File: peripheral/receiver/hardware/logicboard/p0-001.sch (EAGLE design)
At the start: 14 parts, among them IC1 74LS07N, IC2 LTC485N

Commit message: Clean up of document, schematic, and board design.
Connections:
- net GND: no longer JP1.3, MIDIOUT.3
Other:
- note added: "NC"
- note removed: "MIDI Receiver Selector"
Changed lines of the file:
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@@
 <setting verticaltext="up"/>
 </settings>
-<grid distance="0.1" unitdist="inch" unit="inch" style="dots" multiple="1" display="yes" altdistance="0.01" altunitdist="inch" altunit="inch"/>
+<grid distance="0.1" unitdist="inch" unit="inch" style="lines" multiple="1" display="no" altdistance="0.01" altunitdist="inch" altunit="inch"/>
 <layers>
 <layer number="1" name="Top" color="4" fill="1" visible="no" active="no"/>
@@
 <text x="38.1" y="139.7" size="1.778" layer="97" rot="R90">GND</text>
 <text x="40.64" y="139.7" size="1.778" layer="97" rot="R90">External Vcc</text>
-<text x="35.56" y="139.7" size="1.778" layer="97" rot="R90">MIDI Receiver Selector</text>
+<text x="35.56" y="139.7" size="1.778" layer="97" rot="R90">NC</text>
 <text x="33.02" y="139.7" size="1.778" layer="97" rot="R90">MIDI OUT Send</text>
 <text x="30.48" y="139.7" size="1.778" layer="97" rot="R90">MIDI OUT Return</text>
@@
 <wire x1="38.1" y1="116.84" x2="50.8" y2="116.84" width="0.1524" layer="91"/>
 <wire x1="50.8" y1="116.84" x2="50.8" y2="88.9" width="0.1524" layer="91"/>
-<wire x1="38.1" y1="134.62" x2="38.1" y2="121.92" width="0.1524" layer="91"/>
+<wire x1="38.1" y1="134.62" x2="38.1" y2="116.84" width="0.1524" layer="91"/>
 <junction x="38.1" y="116.84"/>
 <pinref part="JP1" gate="A" pin="2"/>
-<pinref part="MIDIOUT" gate="G$1" pin="3"/>
-<pinref part="JP1" gate="A" pin="3"/>
-<wire x1="38.1" y1="121.92" x2="38.1" y2="116.84" width="0.1524" layer="91"/>
-<wire x1="35.56" y1="134.62" x2="35.56" y2="121.92" width="0.1524" layer="91"/>
-<wire x1="35.56" y1="121.92" x2="25.4" y2="121.92" width="0.1524" layer="91"/>
-<wire x1="25.4" y1="121.92" x2="25.4" y2="104.14" width="0.1524" layer="91"/>
-<wire x1="25.4" y1="104.14" x2="27.94" y2="104.14" width="0.1524" layer="91"/>
-<wire x1="38.1" y1="121.92" x2="35.56" y2="121.92" width="0.1524" layer="91"/>
-<junction x="38.1" y="121.92"/>
-<junction x="35.56" y="121.92"/>
-</segment>
-<segment>
+</segment>
+<segment>

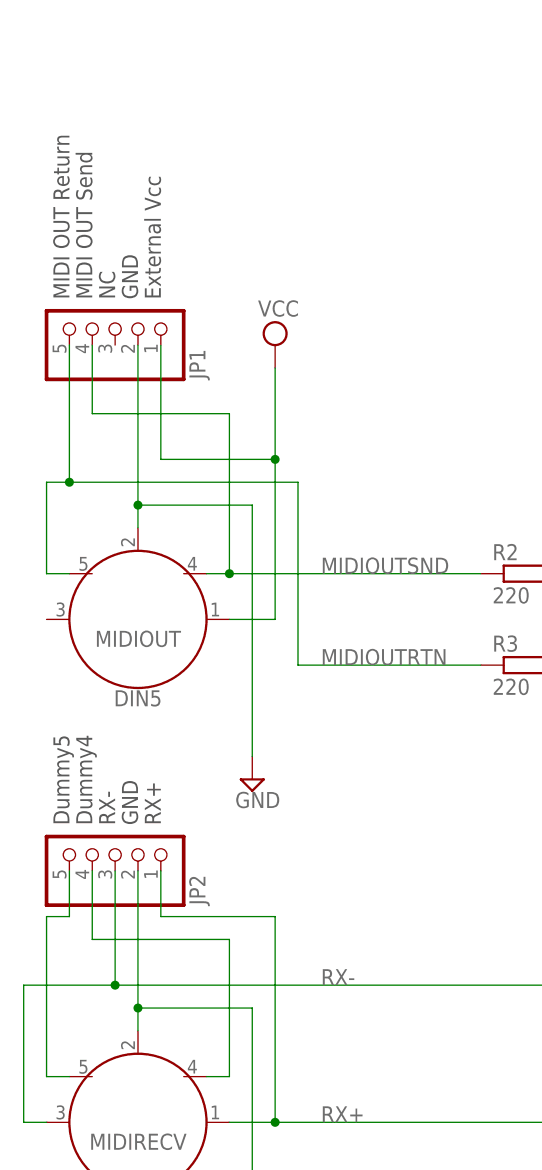
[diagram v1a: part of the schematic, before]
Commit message: Changed connectors of longrange receiver.
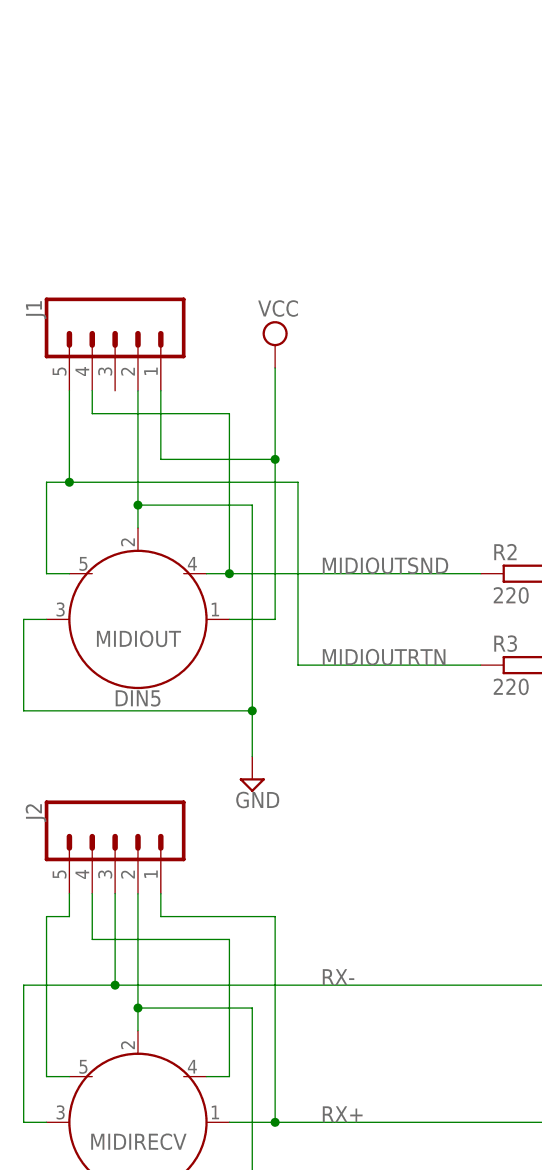
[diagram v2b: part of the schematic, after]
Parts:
- removed JP1, JP2: (no value), pinhead:PINHD-1X5
- added J1, J2: (no value), SparkFun-Connectors:CONN_05JST
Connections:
- net DUMMY4: now also J2.4; no longer JP2.4
- net DUMMY5: now also J2.5; no longer JP2.5
- net GND: now also J1.2, J2.2, MIDIOUT.3; no longer JP1.2, JP2.2
- net MIDIOUTRTN: now also J1.5; no longer JP1.5
- net MIDIOUTSND: now also J1.4; no longer JP1.4
- net RX+: now also J2.1; no longer JP2.1
- net RX-: now also J2.3; no longer JP2.3
- net VCC: now also J1.1; no longer JP1.1
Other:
- note removed: "Dummy4"
- note removed: "Dummy5"
- note removed: "External Vcc"
- note removed: "GND"
- note removed: "MIDI OUT Return"
- note removed: "MIDI OUT Send"
- note removed: "NC"
- note removed: "RX+"
- note removed: "RX-"
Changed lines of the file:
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@@
 <part name="R3" library="resistor" library_urn="urn:adsk.eagle:library:348" deviceset="R-EU_" device="0204/5" package3d_urn="urn:adsk.eagle:package:23488/1" value="220"/>
 <part name="SUPPLY2" library="supply2" library_urn="urn:adsk.eagle:library:372" deviceset="GND" device=""/>
-<part name="JP1" library="pinhead" library_urn="urn:adsk.eagle:library:325" deviceset="PINHD-1X5" device="" package3d_urn="urn:adsk.eagle:package:22469/2"/>
-<part name="JP2" library="pinhead" library_urn="urn:adsk.eagle:library:325" deviceset="PINHD-1X5" device="" package3d_urn="urn:adsk.eagle:package:22469/2"/>
+<part name="J1" library="SparkFun-Connectors" library_urn="urn:adsk.eagle:library:513" deviceset="CONN_05" device="JST" package3d_urn="urn:adsk.eagle:package:38120/1"/>
+<part name="J2" library="SparkFun-Connectors" library_urn="urn:adsk.eagle:library:513" deviceset="CONN_05" device="JST" package3d_urn="urn:adsk.eagle:package:38120/1"/>
 </parts>
 <sheets>
@@
 <plain>
 <text x="215.9" y="20.32" size="1.778" layer="94">Pineapple Zero 1.2.0</text>
-<text x="38.1" y="139.7" size="1.778" layer="97" rot="R90">GND</text>
-<text x="40.64" y="139.7" size="1.778" layer="97" rot="R90">External Vcc</text>
-<text x="35.56" y="139.7" size="1.778" layer="97" rot="R90">NC</text>
-<text x="33.02" y="139.7" size="1.778" layer="97" rot="R90">MIDI OUT Send</text>
-<text x="30.48" y="139.7" size="1.778" layer="97" rot="R90">MIDI OUT Return</text>
-<text x="40.64" y="81.28" size="1.778" layer="97" rot="R90">RX+</text>
-<text x="35.56" y="81.28" size="1.778" layer="97" rot="R90">RX-</text>
-<text x="38.1" y="81.28" size="1.778" layer="97" rot="R90">GND</text>
-<text x="33.02" y="81.28" size="1.778" layer="97" rot="R90">Dummy4</text>
-<text x="30.48" y="81.28" size="1.778" layer="97" rot="R90">Dummy5</text>
 </plain>
 <instances>
@@
 <attribute name="VALUE" x="48.895" y="29.845" size="1.778" layer="96"/>
 </instance>
-<instance part="JP1" gate="A" x="35.56" y="137.16" smashed="yes" rot="MR90">
-<attribute name="NAME" x="43.815" y="130.81" size="1.778" layer="95" rot="MR90"/>
-<attribute name="VALUE" x="25.4" y="130.81" size="1.778" layer="96" rot="MR90"/>
-</instance>
-<instance part="JP2" gate="A" x="35.56" y="78.74" smashed="yes" rot="MR90">
-<attribute name="NAME" x="43.815" y="72.39" size="1.778" layer="95" rot="MR90"/>
-<attribute name="VALUE" x="25.4" y="72.39" size="1.778" layer="96" rot="MR90"/>
+<instance part="J1" gate="G$1" x="35.56" y="137.16" smashed="yes" rot="MR270">
+<attribute name="VALUE" x="45.466" y="139.7" size="1.778" layer="96" font="vector" rot="MR270"/>
+<attribute name="NAME" x="27.432" y="139.7" size="1.778" layer="95" font="vector" rot="MR270"/>
+</instance>
+<instance part="J2" gate="G$1" x="35.56" y="81.28" smashed="yes" rot="MR270">
+<attribute name="VALUE" x="45.466" y="83.82" size="1.778" layer="96" font="vector" rot="MR270"/>
+<attribute name="NAME" x="27.432" y="83.82" size="1.778" layer="95" font="vector" rot="MR270"/>
 </instance>
 </instances>
@@
 <pinref part="SUPPLY1" gate="GND" pin="GND"/>
 <wire x1="38.1" y1="116.84" x2="50.8" y2="116.84" width="0.1524" layer="91"/>
-<wire x1="50.8" y1="116.84" x2="50.8" y2="88.9" width="0.1524" layer="91"/>
-<wire x1="38.1" y1="134.62" x2="38.1" y2="116.84" width="0.1524" layer="91"/>
+<wire x1="50.8" y1="116.84" x2="50.8" y2="93.98" width="0.1524" layer="91"/>
+<wire x1="50.8" y1="93.98" x2="50.8" y2="88.9" width="0.1524" layer="91"/>
+<wire x1="38.1" y1="129.54" x2="38.1" y2="116.84" width="0.1524" layer="91"/>
 <junction x="38.1" y="116.84"/>
-<pinref part="JP1" gate="A" pin="2"/>
+<wire x1="50.8" y1="93.98" x2="25.4" y2="93.98" width="0.1524" layer="91"/>
+<junction x="50.8" y="93.98"/>
+<pinref part="MIDIOUT" gate="G$1" pin="3"/>
+<wire x1="27.94" y1="104.14" x2="25.4" y2="104.14" width="0.1524" layer="91"/>
+<wire x1="25.4" y1="93.98" x2="25.4" y2="104.14" width="0.1524" layer="91"/>
+<pinref part="J1" gate="G$1" pin="2"/>
 </segment>
 <segment>
@@
 <wire x1="38.1" y1="60.96" x2="50.8" y2="60.96" width="0.1524" layer="91"/>
 <wire x1="50.8" y1="60.96" x2="50.8" y2="35.56" width="0.1524" layer="91"/>
-<wire x1="38.1" y1="76.2" x2="38.1" y2="60.96" width="0.1524" layer="91"/>
+<wire x1="38.1" y1="73.66" x2="38.1" y2="60.96" width="0.1524" layer="91"/>
 <junction x="38.1" y="60.96"/>
-<pinref part="JP2" gate="A" pin="2"/>
+<pinref part="J2" gate="G$1" pin="2"/>
 </segment>
 </net>
@@
 <wire x1="53.34" y1="121.92" x2="40.64" y2="121.92" width="0.1524" layer="91"/>
 <junction x="53.34" y="121.92"/>
-<wire x1="40.64" y1="134.62" x2="40.64" y2="121.92" width="0.1524" layer="91"/>
-<pinref part="JP1" gate="A" pin="1"/>
+<wire x1="40.64" y1="129.54" x2="40.64" y2="121.92" width="0.1524" layer="91"/>
+<pinref part="J1" gate="G$1" pin="1"/>
 </segment>
 <segment>
@@
 <wire x1="142.24" y1="48.26" x2="147.32" y2="48.26" width="0.1524" layer="91"/>
 <wire x1="147.32" y1="48.26" x2="147.32" y2="96.52" width="0.1524" layer="91"/>
-<wire x1="40.64" y1="76.2" x2="40.64" y2="71.12" width="0.1524" layer="91"/>
+<wire x1="40.64" y1="73.66" x2="40.64" y2="71.12" width="0.1524" layer="91"/>
 <wire x1="40.64" y1="71.12" x2="53.34" y2="71.12" width="0.1524" layer="91"/>
 <wire x1="53.34" y1="71.12" x2="53.34" y2="48.26" width="0.1524" layer="91"/>
 <junction x="53.34" y="48.26"/>
-<pinref part="JP2" gate="A" pin="1"/>
 <pinref part="R1" gate="G$1" pin="1"/>
 <wire x1="142.24" y1="50.8" x2="142.24" y2="48.26" width="0.1524" layer="91"/>
 <junction x="142.24" y="48.26"/>
 <label x="58.42" y="48.26" size="1.778" layer="95"/>
+<pinref part="J2" gate="G$1" pin="1"/>
 </segment>
 </net>
@@
 <wire x1="27.94" y1="48.26" x2="25.4" y2="48.26" width="0.1524" layer="91"/>
 <wire x1="25.4" y1="48.26" x2="25.4" y2="63.5" width="0.1524" layer="91"/>
-<wire x1="35.56" y1="76.2" x2="35.56" y2="63.5" width="0.1524" layer="91"/>
+<wire x1="35.56" y1="73.66" x2="35.56" y2="63.5" width="0.1524" layer="91"/>
 <junction x="35.56" y="63.5"/>
-<pinref part="JP2" gate="A" pin="3"/>
 <pinref part="R1" gate="G$1" pin="2"/>
 <wire x1="142.24" y1="60.96" x2="142.24" y2="63.5" width="0.1524" layer="91"/>
 <junction x="142.24" y="63.5"/>
 <label x="58.42" y="63.5" size="1.778" layer="95"/>
+<pinref part="J2" gate="G$1" pin="3"/>
 </segment>
 </net>
@@
 <wire x1="76.2" y1="109.22" x2="48.26" y2="109.22" width="0.1524" layer="91"/>
 <wire x1="48.26" y1="109.22" x2="45.72" y2="109.22" width="0.1524" layer="91"/>
-<wire x1="33.02" y1="134.62" x2="33.02" y2="127" width="0.1524" layer="91"/>
+<wire x1="33.02" y1="129.54" x2="33.02" y2="127" width="0.1524" layer="91"/>
 <wire x1="33.02" y1="127" x2="48.26" y2="127" width="0.1524" layer="91"/>
 <wire x1="48.26" y1="127" x2="48.26" y2="109.22" width="0.1524" layer="91"/>
 <junction x="48.26" y="109.22"/>
-<pinref part="JP1" gate="A" pin="4"/>
 <label x="58.42" y="109.22" size="1.778" layer="95"/>
+<pinref part="J1" gate="G$1" pin="4"/>
 </segment>
 </net>
@@
 <pinref part="R3" gate="G$1" pin="1"/>
 <wire x1="55.88" y1="99.06" x2="76.2" y2="99.06" width="0.1524" layer="91"/>
-<wire x1="30.48" y1="134.62" x2="30.48" y2="119.38" width="0.1524" layer="91"/>
+<wire x1="30.48" y1="129.54" x2="30.48" y2="119.38" width="0.1524" layer="91"/>
 <junction x="30.48" y="119.38"/>
-<pinref part="JP1" gate="A" pin="5"/>
 <label x="58.42" y="99.06" size="1.778" layer="95"/>
+<pinref part="J1" gate="G$1" pin="5"/>
 </segment>
 </net>
@@
 <wire x1="48.26" y1="53.34" x2="48.26" y2="68.58" width="0.1524" layer="91"/>
 <wire x1="48.26" y1="68.58" x2="33.02" y2="68.58" width="0.1524" layer="91"/>
-<wire x1="33.02" y1="68.58" x2="33.02" y2="76.2" width="0.1524" layer="91"/>
-<pinref part="JP2" gate="A" pin="4"/>
+<wire x1="33.02" y1="68.58" x2="33.02" y2="73.66" width="0.1524" layer="91"/>
+<pinref part="J2" gate="G$1" pin="4"/>
 </segment>
 </net>
@@
 <wire x1="27.94" y1="53.34" x2="27.94" y2="71.12" width="0.1524" layer="91"/>
 <wire x1="27.94" y1="71.12" x2="30.48" y2="71.12" width="0.1524" layer="91"/>
-<wire x1="30.48" y1="71.12" x2="30.48" y2="76.2" width="0.1524" layer="91"/>
-<pinref part="JP2" gate="A" pin="5"/>
-</segment>
-</net>
+<wire x1="30.48" y1="71.12" x2="30.48" y2="73.66" width="0.1524" layer="91"/>
+<pinref part="J2" gate="G$1" pin="5"/>
+</segment>
+</net>
